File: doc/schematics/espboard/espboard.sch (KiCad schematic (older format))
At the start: 14 parts, among them J1 PWR, J2 Stripe Data, J3 RPi Serial / Boot Btn, J4 Upper Board, U1 ESP32DEVKITV1, U2 SN74HCT245N

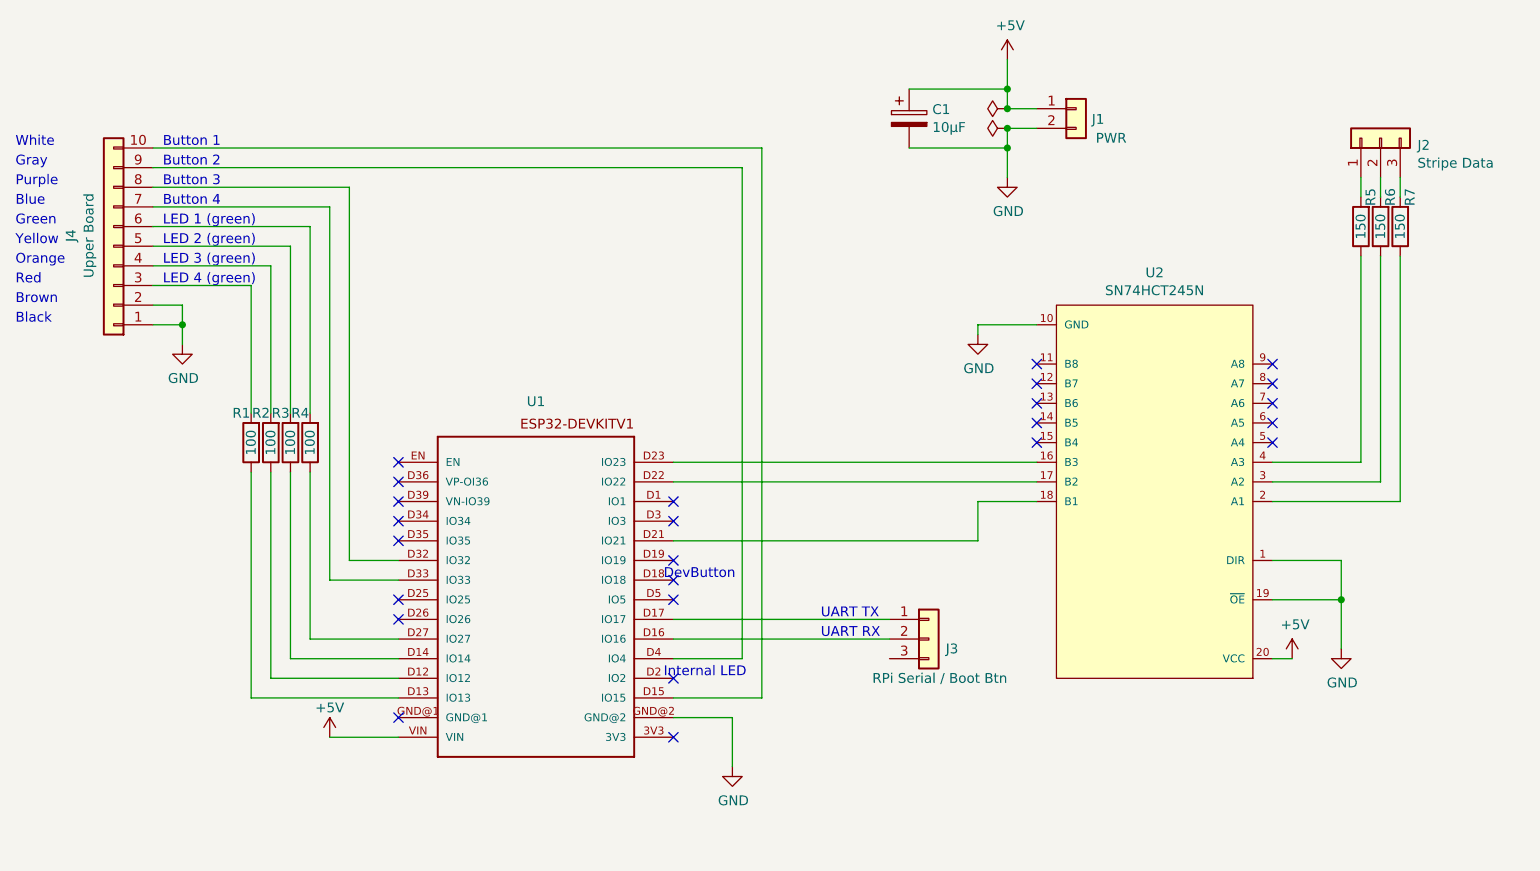
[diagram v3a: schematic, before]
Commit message: Partyraum schematics: Changed pinning for easier layout on perfboard
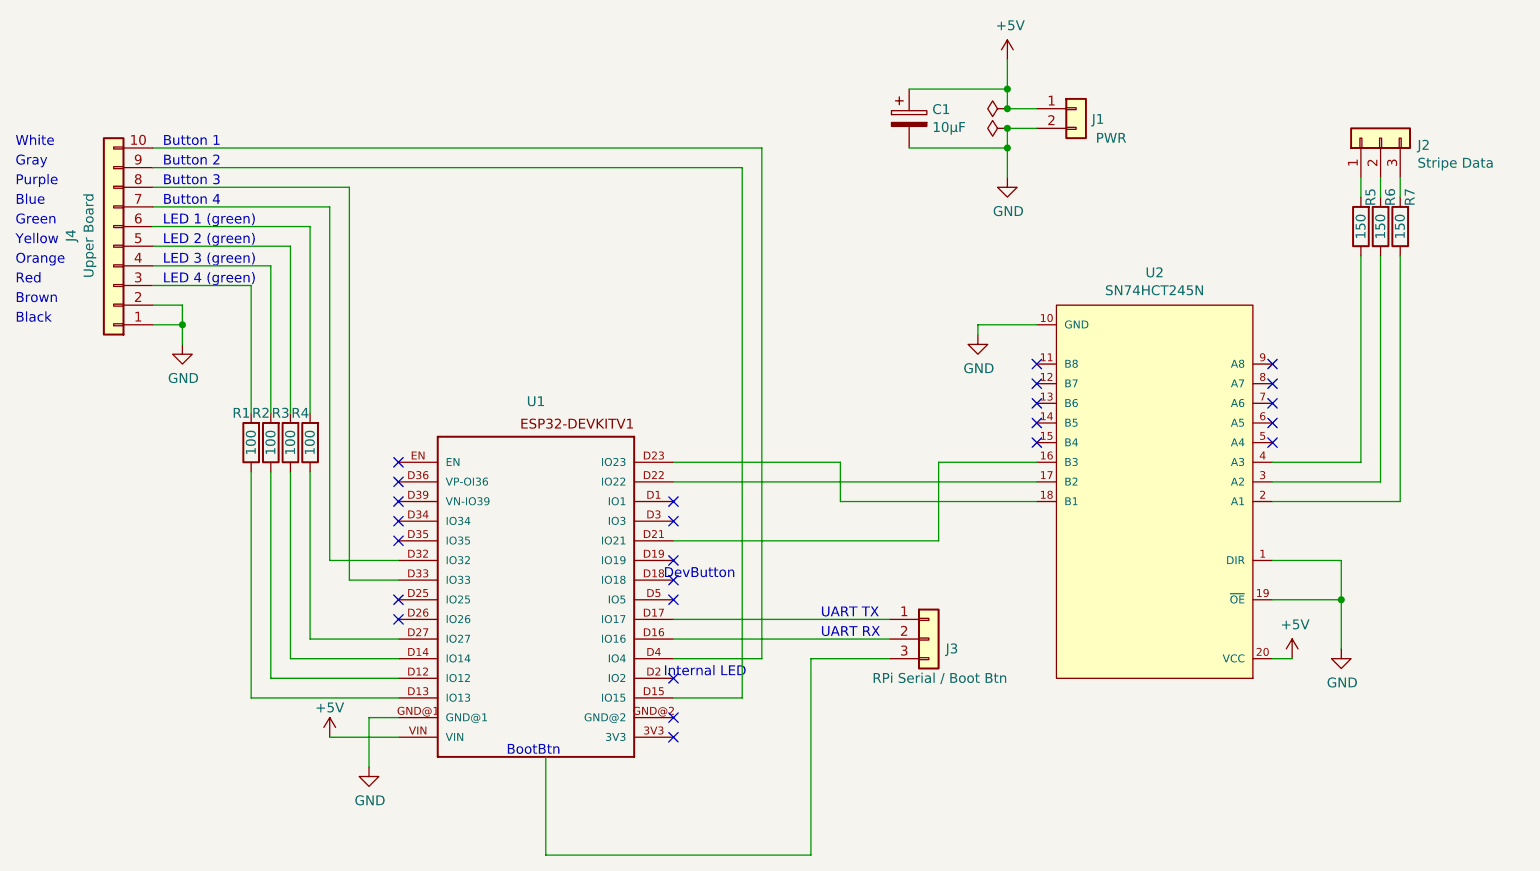
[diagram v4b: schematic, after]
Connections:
- net GND: now also U1.GND@1; no longer U1.GND@2
- net at J4.10 (Pin_10): now also U1.D4 (IO4); no longer U1.D15 (IO15)
- net at J4.7 (Pin_7): now also U1.D32 (IO32); no longer U1.D33 (IO33)
- net at J4.8 (Pin_8): now also U1.D33 (IO33); no longer U1.D32 (IO32)
- net at J4.9 (Pin_9): now also U1.D15 (IO15); no longer U1.D4 (IO4)
- net at U2.16 (B3): now also U1.D21 (IO21); no longer U1.D23 (IO23)
- net at U2.18 (B1): now also U1.D23 (IO23); no longer U1.D21 (IO21)
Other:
- note added: "BootBtn"
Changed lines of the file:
@@
 	1    0    0    -1
 $EndComp
-Wire Wire Line
-	5050 4400 4750 4400
 $Comp
 L Connector_Generic:Conn_01x03 J2
@@
 UART RX
 Wire Wire Line
-	3350 3600 3100 3600
-Wire Wire Line
-	3100 3600 3100 1700
-Wire Wire Line
 	3100 1700 2100 1700
 Wire Wire Line
 	2100 1800 3000 1800
 Wire Wire Line
-	3000 1800 3000 3700
-Wire Wire Line
-	3000 3700 3350 3700
+	3000 1800 3000 3600
 Wire Wire Line
 	3350 4000 2900 4000
@@
 	2100 1600 5100 1600
 Wire Wire Line
-	5100 1600 5100 4100
-Wire Wire Line
-	5100 4100 4750 4100
-Wire Wire Line
 	2100 1500 5200 1500
 Wire Wire Line
-	5200 1500 5200 4300
-Wire Wire Line
-	5200 4300 4750 4300
+	5200 1500 5200 4100
 Text Notes 4700 4200 0    50   ~ 0
 Internal LED
@@
 	8350 1650 8350 1750
 Wire Wire Line
-	4750 3500 6300 3500
-Wire Wire Line
-	6300 3500 6300 3300
-Wire Wire Line
 	6300 2450 6300 2400
 Wire Wire Line
@@
 	8150 3600 7800 3600
 Wire Wire Line
-	4750 3100 6600 3100
-Wire Wire Line
 	4750 3200 6600 3200
-Wire Wire Line
-	6300 3300 6600 3300
 Wire Wire Line
 	7800 3800 8150 3800
@@
 NoConn ~ 3350 3200
 NoConn ~ 3350 3100
-NoConn ~ 3350 4400
 $Comp
 L power:PWR_FLAG #FLG0102
@@
 NoConn ~ 4750 4200
 Wire Wire Line
-	5050 4650 5050 4400
-Wire Wire Line
 	3000 4500 3350 4500
 $Comp
@@
 L power:GND #PWR0101
 U 1 1 5F7CC7B9
-P 5050 4650
-F 0 "#PWR0101" H 5050 4400 50  0001 C CNN
-F 1 "GND" H 5055 4477 50  0000 C CNN
-F 2 "" H 5050 4650 50  0001 C CNN
-F 3 "" H 5050 4650 50  0001 C CNN
-	1    5050 4650
+P 3200 4650
+F 0 "#PWR0101" H 3200 4400 50  0001 C CNN
+F 1 "GND" H 3205 4477 50  0000 C CNN
+F 2 "" H 3200 4650 50  0001 C CNN
+F 3 "" H 3200 4650 50  0001 C CNN
+	1    3200 4650
 	1    0    0    -1
 $EndComp
@@
 Text Notes 1400 1500 0    50   ~ 0
 White
+Wire Wire Line
+	5850 4100 5450 4100
+Wire Wire Line
+	5450 4100 5450 5100
+Wire Wire Line
+	5450 5100 4100 5100
+Wire Wire Line
+	4100 5100 4100 4600
+Text Notes 3900 4600 0    50   ~ 0
+BootBtn
+Wire Wire Line
+	5600 3300 5600 3100
+Wire Wire Line
+	5600 3100 4750 3100
+Wire Wire Line
+	5600 3300 6600 3300
+Wire Wire Line
+	6600 3100 6100 3100
+Wire Wire Line
+	6100 3500 4750 3500
+Wire Wire Line
+	6100 3100 6100 3500
+Wire Wire Line
+	3100 3700 3350 3700
+Wire Wire Line
+	3100 1700 3100 3700
+Wire Wire Line
+	3000 3600 3350 3600
+Wire Wire Line
+	3200 4650 3200 4400
+Wire Wire Line
+	3200 4400 3350 4400
+NoConn ~ 4750 4400
+Wire Wire Line
+	5100 4300 4750 4300
+Wire Wire Line
+	5100 1600 5100 4300
+Wire Wire Line
+	5200 4100 4750 4100
 $EndSCHEMATC
